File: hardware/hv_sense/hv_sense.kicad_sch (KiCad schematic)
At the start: 39 parts, among them J1 Conn_01x02, J2 Conn_01x02, J3 Conn_01x02, J4 Conn_01x02, J5 Conn_01x03, J6 Conn_01x02, J7 Conn_01x04, J8 Conn_01x02, U10 140817141410, U8 TLV274, U9 TL431ACDT

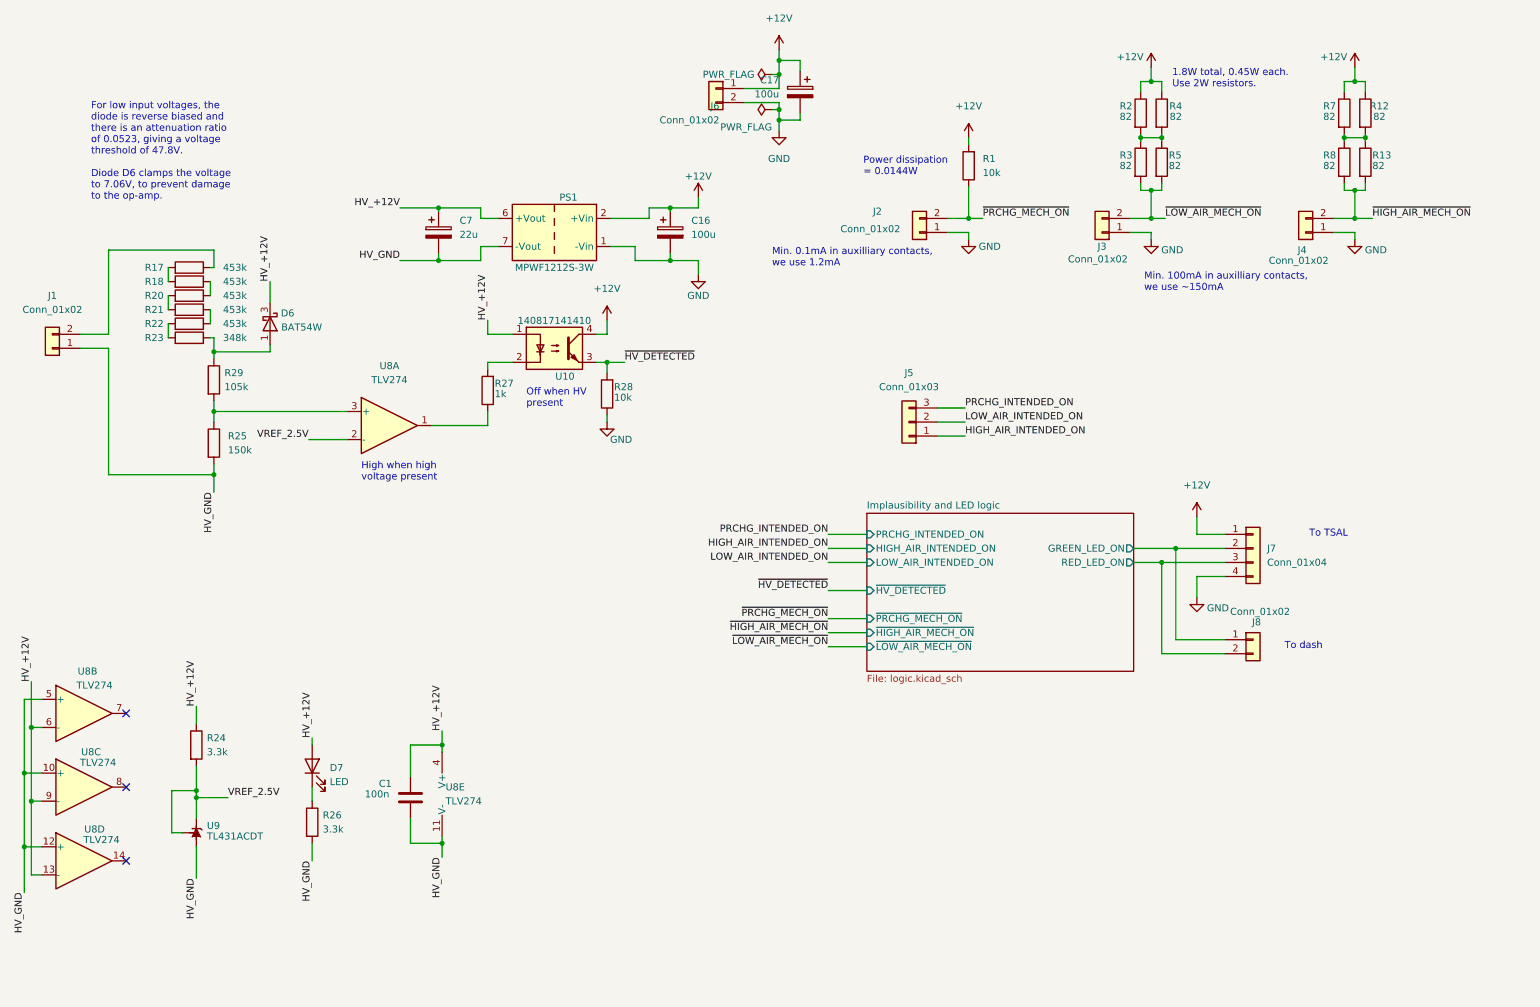
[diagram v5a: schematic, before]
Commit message: Changed connector footprints
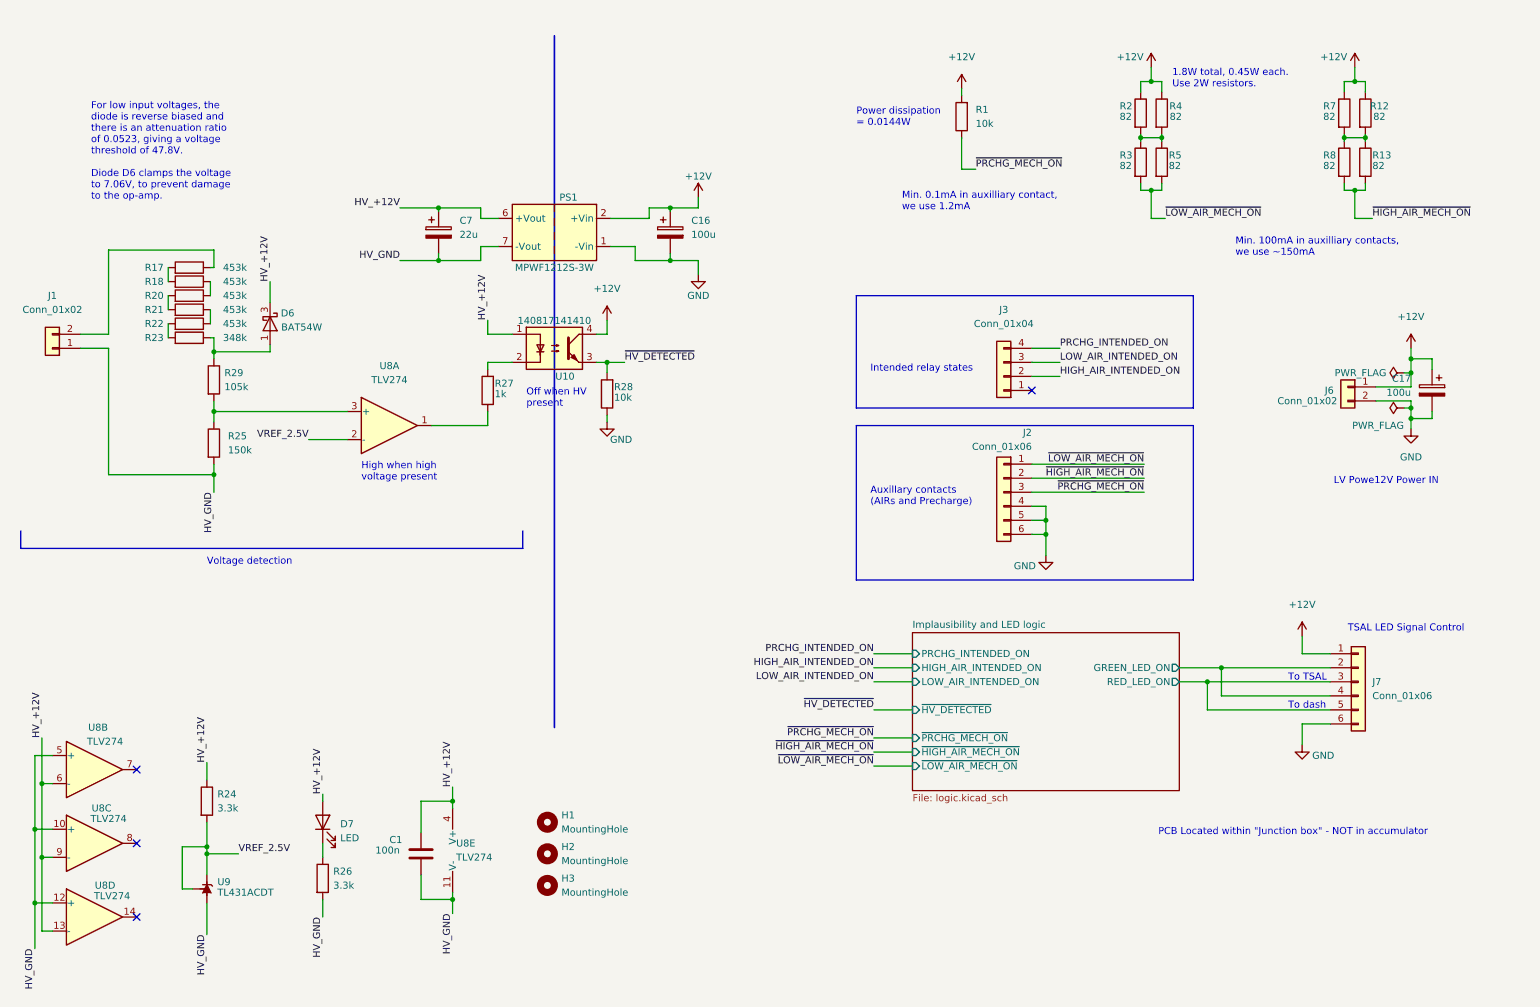
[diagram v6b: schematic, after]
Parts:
- removed J2, J3, J4, J8: Conn_01x02, Connector_Molex:Molex_Micro-Fit_3.0_43650-0200_1x02_P3.00mm_Horizontal, symbol Connector_Generic:Conn_01x02
- removed J5: Conn_01x03, Connector_Molex:Molex_Micro-Fit_3.0_43650-0300_1x03_P3.00mm_Horizontal, symbol Connector_Generic:Conn_01x03
- removed J7: Conn_01x04, Connector_Molex:Molex_Micro-Fit_3.0_43650-0400_1x04_P3.00mm_Horizontal, symbol Connector_Generic:Conn_01x04
- added H1, H2, H3: MountingHole, MountingHole:MountingHole_3.2mm_M3, symbol Mechanical:MountingHole
- added J2, J7: Conn_01x06, footprints:Molex_Micro-Fit_3.0_43045-0612_2x03_P3.00mm_Vertical, symbol Connector_Generic:Conn_01x06
- added J3: Conn_01x04, footprints:Molex_Micro-Fit_3.0_43045-0412_2x02_P3.00mm_Vertical, symbol Connector_Generic:Conn_01x04
- J1, J6: footprint Connector_Molex:Molex_Micro-Fit_3.0_43650-0200_1x02_P3.00mm_Horizontal -> footprints:Molex_Micro-Fit_3.0_43045-0212_2x01_P3.00mm_Vertical
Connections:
- net +12V: now also J7.1 (Pin_1)
- net GND: now also J2.4 (Pin_4), J2.5 (Pin_5), J2.6 (Pin_6), J7.6 (Pin_6)
- net HIGH_AIR_INTENDED_ON: now also J3.2 (Pin_2)
- net Implausibility and LED logic/GREEN_LED_ON: now also J7.2 (Pin_2), J7.4 (Pin_4)
- net Implausibility and LED logic/RED_LED_ON: now also J7.3 (Pin_3), J7.5 (Pin_5)
- net LOW_AIR_INTENDED_ON: now also J3.3 (Pin_3)
- net PRCHG_INTENDED_ON: now also J3.4 (Pin_4)
- net ~{HIGH_AIR_MECH_ON}: now also J2.2 (Pin_2)
- net ~{LOW_AIR_MECH_ON}: now also J2.1 (Pin_1)
- net ~{PRCHG_MECH_ON}: now also J2.3 (Pin_3)
- no-connect marks 3 -> 4
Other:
- note added: "Auxillary contacts (AIRs and Precharge)"
- note added: "Intended relay states"
- note added: "LV Powe12V Power IN"
- note added: "Min. 0.1mA in auxilliary contact, we use 1.2mA"
- note added: "PCB Located within "Junction box" - NOT in accumulator"
- note added: "TSAL LED Signal Control"
- note added: "Voltage detection"
- note removed: "Min. 0.1mA in auxilliary contacts, we use 1.2mA"
- company: (none) -> SUFST - Southampton University Formula Student Team
- title: (none) -> TSAL Sense / Logic - Top level
- moved on the sheet: C1, C17, D7, J6, R1, R24, R26, U8B, U8C, U8D, U8E, U9

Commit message: Added PCB updates
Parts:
- removed PS1: MPWF1212S-3W, footprints:MPWF1212S-3W, symbol Converter_DCDC:ITX1212SA
- added PS1: 0.5S7B_1212S3UP, footprints:0.5S7B_1212S3UP, symbol symbols:0.5S7B_1212S3UP
- added R30, R31, R32: 82, Resistor_SMD:R_2512_6332Metric, symbol Device:R
- R1: value 10k -> 82; footprint Resistor_SMD:R_0603_1608Metric -> Resistor_SMD:R_2512_6332Metric
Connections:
- net +12V: now also R1.1, PS1.1 (+Vin), R31.1; no longer R1.2
- net GND: now also PS1.2 (-Vin)
- net HV_+12V: now also PS1.7 (+Vout)
- net HV_GND: now also PS1.5 (-Vout)
- net ~{PRCHG_MECH_ON}: now also R30.2, R32.2; no longer R1.1
- new net: R1.2, R30.1, R31.2, R32.1
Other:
- note removed: "Min. 0.1mA in auxilliary contact, we use 1.2mA"
- note removed: "Power dissipation = 0.0144W"
